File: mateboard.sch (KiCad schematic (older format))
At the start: 27 parts, among them J1 CONN_02X20, J2 CONN_02X20, P1 POWER, P2 DEVICE, P3 HOST, P4 microSD, Q1 BSS138, Q2 BSS138, Q3 BSS138, Q4 BSS138

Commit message: erc passed, sch first version
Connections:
- wire segments 188 -> 190
- no-connect marks 4 -> 3
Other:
- moved on the sheet: R1

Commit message: wip display connector
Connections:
- wire segments 190 -> 212
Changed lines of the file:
@@
 	1050 4525 900  4525
 Wire Wire Line
-	900  4500 900  4625
+	900  4500 900  4525
+Wire Wire Line
+	900  4525 900  4625
 Wire Wire Line
 	1350 4525 1525 4525
 Wire Wire Line
-	1525 4500 1525 4575
+	1525 4500 1525 4525
+Wire Wire Line
+	1525 4525 1525 4575
 $Sheet
 S 2600 4050 1250 1650
@@
 Connection ~ 9100 700
 Wire Wire Line
-	8625 700  9300 700
+	8625 700  8700 700
+Wire Wire Line
+	8700 700  8800 700
+Wire Wire Line
+	8800 700  8900 700
+Wire Wire Line
+	8900 700  9000 700
+Wire Wire Line
+	9000 700  9100 700
+Wire Wire Line
+	9100 700  9200 700
+Wire Wire Line
+	9200 700  9300 700
 Wire Wire Line
 	9200 700  9200 825
@@
 	9300 1125 9300 1175
 Wire Wire Line
-	8150 1175 9375 1175
-Wire Wire Line
-	8150 1275 9375 1275
+	8150 1175 9300 1175
+Wire Wire Line
+	9300 1175 9375 1175
+Wire Wire Line
+	8150 1275 9200 1275
+Wire Wire Line
+	9200 1275 9375 1275
 Wire Wire Line
 	9200 1275 9200 1125
 Wire Wire Line
-	8150 1375 9375 1375
+	8150 1375 9100 1375
+Wire Wire Line
+	9100 1375 9375 1375
 Wire Wire Line
 	9100 1375 9100 1125
@@
 	8700 1475 8700 700
 Wire Wire Line
-	8150 1575 9375 1575
+	8150 1575 9000 1575
+Wire Wire Line
+	9000 1575 9375 1575
 Wire Wire Line
 	9000 1575 9000 1125
@@
 $EndComp
 Wire Wire Line
-	9300 1675 9300 2175
+	9300 1675 9300 2125
+Wire Wire Line
+	9300 2125 9300 2175
 Wire Wire Line
 	9300 1675 9375 1675
 Wire Wire Line
-	8150 1775 9375 1775
+	8150 1775 8900 1775
+Wire Wire Line
+	8900 1775 9375 1775
 Wire Wire Line
 	8900 1775 8900 1125
 Wire Wire Line
-	8150 1875 9375 1875
+	8150 1875 8800 1875
+Wire Wire Line
+	8800 1875 9375 1875
 Wire Wire Line
 	8800 1875 8800 1125
@@
 Connection ~ 8700 700
 Wire Wire Line
-	8625 1125 8625 3425
+	8625 1125 8625 2025
+Wire Wire Line
+	8625 2025 8625 3425
 Wire Wire Line
 	9375 2125 9300 2125
@@
 	6800 3425 6900 3425
 Wire Wire Line
-	5850 2325 5850 3425
+	5850 2325 5850 3050
+Wire Wire Line
+	5850 3050 5850 3425
 Wire Wire Line
 	5850 2325 5725 2325
@@
 I2C0_SCL
 $Sheet
-S 6900 5650 1250 700
+S 6900 5650 1250 800
 U 58BD360A
-F0 "Boot Config" 60
+F0 "Boot Config-LCD" 60
 F1 "sysboot.sch" 60
 F2 "GPIO2_23" B R 8150 5850 60
@@
 F4 "GPIO2_24" B R 8150 5950 60
 F5 "GPIO2_25" B R 8150 6050 60
+F6 "HDMI_INT" O L 6900 5750 60
+F7 "CSDA" B L 6900 5950 60
+F8 "CSCL" I L 6900 6050 60
+F9 "ACLK" I R 8150 6150 60
+F10 "AP0" I R 8150 6250 60
+F11 "AP1" I R 8150 6350 60
+F12 "HDMICLK_DIS" I L 6900 5850 60
 $EndSheet
 Wire Wire Line
@@
 GPIO1_16
 Wire Wire Line
-	6900 2900 6475 2900
+	6050 2900 6900 2900
 Text Label 6475 2900 0    60   ~ 0
 GPIO1_27
 Wire Wire Line
-	6900 3000 6475 3000
+	6150 3000 6900 3000
 Text Label 6475 3000 0    60   ~ 0
 GPIO1_25
@@
 USB1_VBUS
 Wire Wire Line
-	9950 5525 9450 5525
+	9950 5525 9900 5525
+Wire Wire Line
+	9900 5525 9450 5525
 Text Label 9450 5525 0    60   ~ 0
 VBAT
@@
 UART4_TXD
 $Comp
-L GNDD #PWR?
+L GNDD #PWR042
 U 1 1 58C8D040
 P 9950 5425
-F 0 "#PWR?" H 9950 5175 50  0001 C CNN
+F 0 "#PWR042" H 9950 5175 50  0001 C CNN
 F 1 "GNDD" V 9950 5200 50  0000 C CNN
 F 2 "" H 9950 5425 50  0000 C CNN
@@
 	0    1    1    0
 $EndComp
+Wire Wire Line
+	6900 5750 6150 5750
+Wire Wire Line
+	6150 5750 6150 3000
+Wire Wire Line
+	6050 2900 6050 5850
+Wire Wire Line
+	6050 5850 6900 5850
 $EndSCHEMATC

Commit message: add display connector, bom generated, sch second version
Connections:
- wire segments 212 -> 202
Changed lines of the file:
@@
 	1050 4525 900  4525
 Wire Wire Line
-	900  4500 900  4525
-Wire Wire Line
-	900  4525 900  4625
+	900  4500 900  4625
 Wire Wire Line
 	1350 4525 1525 4525
 Wire Wire Line
-	1525 4500 1525 4525
-Wire Wire Line
-	1525 4525 1525 4575
+	1525 4500 1525 4575
 $Sheet
 S 2600 4050 1250 1650
@@
 F10 "GPIO0_7" B R 5725 1225 60
 F11 "CLKOUT2" O R 5725 2325 60
+F12 "CLKOUT1" O R 5725 2225 60
 $EndSheet
 $Sheet
@@
 Connection ~ 9100 700
 Wire Wire Line
-	8625 700  8700 700
-Wire Wire Line
-	8700 700  8800 700
-Wire Wire Line
-	8800 700  8900 700
-Wire Wire Line
-	8900 700  9000 700
-Wire Wire Line
-	9000 700  9100 700
-Wire Wire Line
-	9100 700  9200 700
-Wire Wire Line
-	9200 700  9300 700
+	8625 700  9300 700
 Wire Wire Line
 	9200 700  9200 825
@@
 	9300 1125 9300 1175
 Wire Wire Line
-	8150 1175 9300 1175
-Wire Wire Line
-	9300 1175 9375 1175
-Wire Wire Line
-	8150 1275 9200 1275
-Wire Wire Line
-	9200 1275 9375 1275
+	8150 1175 9375 1175
+Wire Wire Line
+	8150 1275 9375 1275
 Wire Wire Line
 	9200 1275 9200 1125
 Wire Wire Line
-	8150 1375 9100 1375
-Wire Wire Line
-	9100 1375 9375 1375
+	8150 1375 9375 1375
 Wire Wire Line
 	9100 1375 9100 1125
@@
 	8700 1475 8700 700
 Wire Wire Line
-	8150 1575 9000 1575
-Wire Wire Line
-	9000 1575 9375 1575
+	8150 1575 9375 1575
 Wire Wire Line
 	9000 1575 9000 1125
@@
 $EndComp
 Wire Wire Line
-	9300 1675 9300 2125
-Wire Wire Line
-	9300 2125 9300 2175
+	9300 1675 9300 2175
 Wire Wire Line
 	9300 1675 9375 1675
 Wire Wire Line
-	8150 1775 8900 1775
-Wire Wire Line
-	8900 1775 9375 1775
+	8150 1775 9375 1775
 Wire Wire Line
 	8900 1775 8900 1125
 Wire Wire Line
-	8150 1875 8800 1875
-Wire Wire Line
-	8800 1875 9375 1875
+	8150 1875 9375 1875
 Wire Wire Line
 	8800 1875 8800 1125
@@
 Connection ~ 8700 700
 Wire Wire Line
-	8625 1125 8625 2025
-Wire Wire Line
-	8625 2025 8625 3425
+	8625 1125 8625 3425
 Wire Wire Line
 	9375 2125 9300 2125
@@
 	6800 3425 6900 3425
 Wire Wire Line
-	5850 2325 5850 3050
-Wire Wire Line
-	5850 3050 5850 3425
+	5850 2325 5850 3425
 Wire Wire Line
 	5850 2325 5725 2325
@@
 F11 "AP1" I R 8150 6350 60
 F12 "HDMICLK_DIS" I L 6900 5850 60
+F13 "OSC_IN" I L 6900 6150 60
 $EndSheet
 Wire Wire Line
@@
 AIN6
 Wire Wire Line
-	8150 5750 8575 5750
-Text Label 8575 5750 2    60   ~ 0
+	8150 5750 8650 5750
+Text Label 8650 5750 2    60   ~ 0
 GPIO2_22
 Wire Wire Line
-	8150 5850 8575 5850
-Text Label 8575 5850 2    60   ~ 0
+	8150 5850 8650 5850
+Text Label 8650 5850 2    60   ~ 0
 GPIO2_23
 Wire Wire Line
-	8150 5950 8575 5950
-Text Label 8575 5950 2    60   ~ 0
+	8150 5950 8650 5950
+Text Label 8650 5950 2    60   ~ 0
 GPIO2_24
 Wire Wire Line
-	8150 6050 8575 6050
-Text Label 8575 6050 2    60   ~ 0
+	8150 6050 8650 6050
+Text Label 8650 6050 2    60   ~ 0
 GPIO2_25
 $Comp
@@
 USB1_VBUS
 Wire Wire Line
-	9950 5525 9900 5525
-Wire Wire Line
-	9900 5525 9450 5525
+	9450 5525 9950 5525
 Text Label 9450 5525 0    60   ~ 0
 VBAT
@@
 Wire Wire Line
 	6050 5850 6900 5850
+Wire Wire Line
+	6900 5950 6400 5950
+Wire Wire Line
+	6400 6050 6900 6050
+Text Label 6400 6050 0    60   ~ 0
+I2C0_SDA
+Text Label 6400 5950 0    60   ~ 0
+I2C0_SCL
+Wire Wire Line
+	5725 2225 6250 2225
+Wire Wire Line
+	6250 2225 6250 6150
+Wire Wire Line
+	6250 6150 6900 6150
+Text Label 8650 6150 2    60   ~ 0
+SPI1_SCLK
+Wire Wire Line
+	8650 6150 8150 6150
+Text Label 8650 6250 2    60   ~ 0
+SPI1_MISO
+Wire Wire Line
+	8650 6250 8150 6250
+Text Label 8650 6350 2    60   ~ 0
+SPI1_CS0
+Wire Wire Line
+	8650 6350 8150 6350
 $EndSCHEMATC

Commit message: wip sch
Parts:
- removed D1, D2, D3, D4: LTST-C191TBKT, symbol LED
- removed Q1, Q2, Q3, Q4: BSS138, TO_SOT_Packages_SMD:SOT-23, symbol BSS138
- removed R2, R3, R4, R5: 1k, symbol R
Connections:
- wire segments 202 -> 198
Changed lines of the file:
@@
 LIBS:74lvc1g07dck
 LIBS:wl1835modgbmoct
+LIBS:osd335x
 LIBS:mateboard-cache
 EELAYER 25 0
@@
 	5850 3425 6500 3425
 Connection ~ 5850 3050
-$Comp
-L BSS138 Q1
-U 1 1 58BD6236
-P 1125 7300
-F 0 "Q1" H 1325 7375 50  0000 L CNN
-F 1 "BSS138" H 1325 7300 50  0000 L CNN
-F 2 "TO_SOT_Packages_SMD:SOT-23" H 1325 7225 50  0001 L CIN
-F 3 "" H 1125 7300 50  0001 L CNN
-	1    1125 7300
-	1    0    0    -1
-$EndComp
-Wire Wire Line
-	625  7350 925  7350
-$Comp
-L GNDD #PWR014
-U 1 1 58BD623E
-P 1225 7500
-F 0 "#PWR014" H 1225 7250 50  0001 C CNN
-F 1 "GNDD" H 1225 7350 50  0000 C CNN
-F 2 "" H 1225 7500 50  0000 C CNN
-F 3 "" H 1225 7500 50  0000 C CNN
-	1    1225 7500
-	1    0    0    -1
-$EndComp
-$Comp
-L LED D1
-U 1 1 58BD6244
-P 1225 6950
-F 0 "D1" H 1225 7150 50  0000 C CNN
-F 1 "LTST-C191TBKT" H 1225 7075 50  0000 C CNN
-F 2 "" H 1225 6950 50  0000 C CNN
-F 3 "" H 1225 6950 50  0000 C CNN
-	1    1225 6950
-	0    -1   -1   0
-$EndComp
-$Comp
-L R R2
-U 1 1 58BD624B
-P 1225 6650
-F 0 "R2" V 1275 6800 50  0000 C CNN
-F 1 "1k" V 1225 6650 50  0000 C CNN
-F 2 "" V 1155 6650 50  0000 C CNN
-F 3 "" H 1225 6650 50  0000 C CNN
-	1    1225 6650
-	1    0    0    -1
-$EndComp
-Text Label 625  7350 0    60   ~ 0
-USR0
-$Comp
-L VDD_3V3B #PWR015
-U 1 1 58BD685D
-P 1225 6500
-F 0 "#PWR015" H 1225 6350 50  0001 C CNN
-F 1 "VDD_3V3B" H 1225 6650 50  0000 C CNN
-F 2 "" H 1225 6500 50  0000 C CNN
-F 3 "" H 1225 6500 50  0000 C CNN
-	1    1225 6500
-	1    0    0    -1
-$EndComp
-$Comp
-L BSS138 Q2
-U 1 1 58BDAD53
-P 2125 7300
-F 0 "Q2" H 2325 7375 50  0000 L CNN
-F 1 "BSS138" H 2325 7300 50  0000 L CNN
-F 2 "TO_SOT_Packages_SMD:SOT-23" H 2325 7225 50  0001 L CIN
-F 3 "" H 2125 7300 50  0001 L CNN
-	1    2125 7300
-	1    0    0    -1
-$EndComp
-Wire Wire Line
-	1625 7350 1925 7350
-$Comp
-L GNDD #PWR016
-U 1 1 58BDAD5A
-P 2225 7500
-F 0 "#PWR016" H 2225 7250 50  0001 C CNN
-F 1 "GNDD" H 2225 7350 50  0000 C CNN
-F 2 "" H 2225 7500 50  0000 C CNN
-F 3 "" H 2225 7500 50  0000 C CNN
-	1    2225 7500
-	1    0    0    -1
-$EndComp
-$Comp
-L LED D2
-U 1 1 58BDAD60
-P 2225 6950
-F 0 "D2" H 2225 7150 50  0000 C CNN
-F 1 "LTST-C191TBKT" H 2225 7075 50  0000 C CNN
-F 2 "" H 2225 6950 50  0000 C CNN
-F 3 "" H 2225 6950 50  0000 C CNN
-	1    2225 6950
-	0    -1   -1   0
-$EndComp
-$Comp
-L R R3
-U 1 1 58BDAD66
-P 2225 6650
-F 0 "R3" V 2275 6800 50  0000 C CNN
-F 1 "1k" V 2225 6650 50  0000 C CNN
-F 2 "" V 2155 6650 50  0000 C CNN
-F 3 "" H 2225 6650 50  0000 C CNN
-	1    2225 6650
-	1    0    0    -1
-$EndComp
-Text Label 1625 7350 0    60   ~ 0
-USR1
-$Comp
-L VDD_3V3B #PWR017
-U 1 1 58BDAD6D
-P 2225 6500
-F 0 "#PWR017" H 2225 6350 50  0001 C CNN
-F 1 "VDD_3V3B" H 2225 6650 50  0000 C CNN
-F 2 "" H 2225 6500 50  0000 C CNN
-F 3 "" H 2225 6500 50  0000 C CNN
-	1    2225 6500
-	1    0    0    -1
-$EndComp
-$Comp
-L BSS138 Q3
-U 1 1 58BDC8A1
-P 3150 7300
-F 0 "Q3" H 3350 7375 50  0000 L CNN
-F 1 "BSS138" H 3350 7300 50  0000 L CNN
-F 2 "TO_SOT_Packages_SMD:SOT-23" H 3350 7225 50  0001 L CIN
-F 3 "" H 3150 7300 50  0001 L CNN
-	1    3150 7300
-	1    0    0    -1
-$EndComp
-Wire Wire Line
-	2650 7350 2950 7350
-$Comp
-L GNDD #PWR018
-U 1 1 58BDC8A8
-P 3250 7500
-F 0 "#PWR018" H 3250 7250 50  0001 C CNN
-F 1 "GNDD" H 3250 7350 50  0000 C CNN
-F 2 "" H 3250 7500 50  0000 C CNN
-F 3 "" H 3250 7500 50  0000 C CNN
-	1    3250 7500
-	1    0    0    -1
-$EndComp
-$Comp
-L LED D3
-U 1 1 58BDC8AE
-P 3250 6950
-F 0 "D3" H 3250 7150 50  0000 C CNN
-F 1 "LTST-C191TBKT" H 3250 7075 50  0000 C CNN
-F 2 "" H 3250 6950 50  0000 C CNN
-F 3 "" H 3250 6950 50  0000 C CNN
-	1    3250 6950
-	0    -1   -1   0
-$EndComp
-$Comp
-L R R4
-U 1 1 58BDC8B4
-P 3250 6650
-F 0 "R4" V 3300 6800 50  0000 C CNN
-F 1 "1k" V 3250 6650 50  0000 C CNN
-F 2 "" V 3180 6650 50  0000 C CNN
-F 3 "" H 3250 6650 50  0000 C CNN
-	1    3250 6650
-	1    0    0    -1
-$EndComp
-Text Label 2650 7350 0    60   ~ 0
-USR2
-$Comp
-L VDD_3V3B #PWR019
-U 1 1 58BDC8BB
-P 3250 6500
-F 0 "#PWR019" H 3250 6350 50  0001 C CNN
-F 1 "VDD_3V3B" H 3250 6650 50  0000 C CNN
-F 2 "" H 3250 6500 50  0000 C CNN
-F 3 "" H 3250 6500 50  0000 C CNN
-	1    3250 6500
-	1    0    0    -1
-$EndComp
-$Comp
-L BSS138 Q4
-U 1 1 58BDC8C1
-P 4150 7300
-F 0 "Q4" H 4350 7375 50  0000 L CNN
-F 1 "BSS138" H 4350 7300 50  0000 L CNN
-F 2 "TO_SOT_Packages_SMD:SOT-23" H 4350 7225 50  0001 L CIN
-F 3 "" H 4150 7300 50  0001 L CNN
-	1    4150 7300
-	1    0    0    -1
-$EndComp
-Wire Wire Line
-	3650 7350 3950 7350
-$Comp
-L GNDD #PWR020
-U 1 1 58BDC8C8
-P 4250 7500
-F 0 "#PWR020" H 4250 7250 50  0001 C CNN
-F 1 "GNDD" H 4250 7350 50  0000 C CNN
-F 2 "" H 4250 7500 50  0000 C CNN
-F 3 "" H 4250 7500 50  0000 C CNN
-	1    4250 7500
-	1    0    0    -1
-$EndComp
-$Comp
-L LED D4
-U 1 1 58BDC8CE
-P 4250 6950
-F 0 "D4" H 4250 7150 50  0000 C CNN
-F 1 "LTST-C191TBKT" H 4250 7075 50  0000 C CNN
-F 2 "" H 4250 6950 50  0000 C CNN
-F 3 "" H 4250 6950 50  0000 C CNN
-	1    4250 6950
-	0    -1   -1   0
-$EndComp
-$Comp
-L R R5
-U 1 1 58BDC8D4
-P 4250 6650
-F 0 "R5" V 4300 6800 50  0000 C CNN
-F 1 "1k" V 4250 6650 50  0000 C CNN
-F 2 "" V 4180 6650 50  0000 C CNN
-F 3 "" H 4250 6650 50  0000 C CNN
-	1    4250 6650
-	1    0    0    -1
-$EndComp
-Text Label 3650 7350 0    60   ~ 0
-USR3
-$Comp
-L VDD_3V3B #PWR021
-U 1 1 58BDC8DB
-P 4250 6500
-F 0 "#PWR021" H 4250 6350 50  0001 C CNN
-F 1 "VDD_3V3B" H 4250 6650 50  0000 C CNN
-F 2 "" H 4250 6500 50  0000 C CNN
-F 3 "" H 4250 6500 50  0000 C CNN
-	1    4250 6500
-	1    0    0    -1
-$EndComp
 Wire Wire Line
 	8150 2050 8400 2050

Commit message: wip sys and power
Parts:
- removed J1, J2: CONN_02X20, symbol CONN_02X20
- removed P1: POWER, symbol USB_OTG-RESCUE-mateboard
- removed P2: DEVICE, symbol USB_OTG-RESCUE-mateboard
- removed P3: HOST, symbol USB_A-RESCUE-mateboard
- removed P4: microSD, symbol microSD
- removed R1: 0.1, Resistors_SMD:R_0805, symbol R
- removed R10, R11, R12, R13, R7, R8, R9: 10k, symbol R
- removed R6: 0R, symbol R
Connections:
- net labels removed: AIN0, AIN1, AIN2, AIN3, AIN4, AIN5, AIN6, GNDA, GNDD, GNDSHIELD, GPIO0_26, GPIO0_27, GPIO0_7, GPIO1_12, GPIO1_13, GPIO1_14, GPIO1_15, GPIO1_16, GPIO1_17, GPIO1_25, GPIO1_27, GPIO1_28, GPIO1_29, GPIO2_0, GPIO2_1, GPIO2_22, GPIO2_23, GPIO2_24, GPIO2_25, GPIO3_19, GPIO3_21, I2C1_SCL, I2C1_SDA, I2C2_SCL, I2C2_SDA, MMC0_CD, PWM1A, PWM1B, PWM2A, PWM2B, SPI1_CS0, SPI1_MISO, SPI1_MOSI, SPI1_SCLK, SYS_5V, TIMER4, TIMER5, TIMER6, TIMER7, UART0_RXD, UART0_TXD, UART1_RXD, UART1_TXD, UART2_RXD, UART2_TXD, UART4_RXD, UART4_TXD, USB0_DM, USB0_DP, USB0_ID, USB1_DM, USB1_DP, USB1_OCn, USB1_VBUS, USB_DC, USR0, USR1, USR2, USR3, VDD_3V3B, VDD_5V, VSS_RTC
- wire segments 198 -> 11
- no-connect marks 3 -> 0

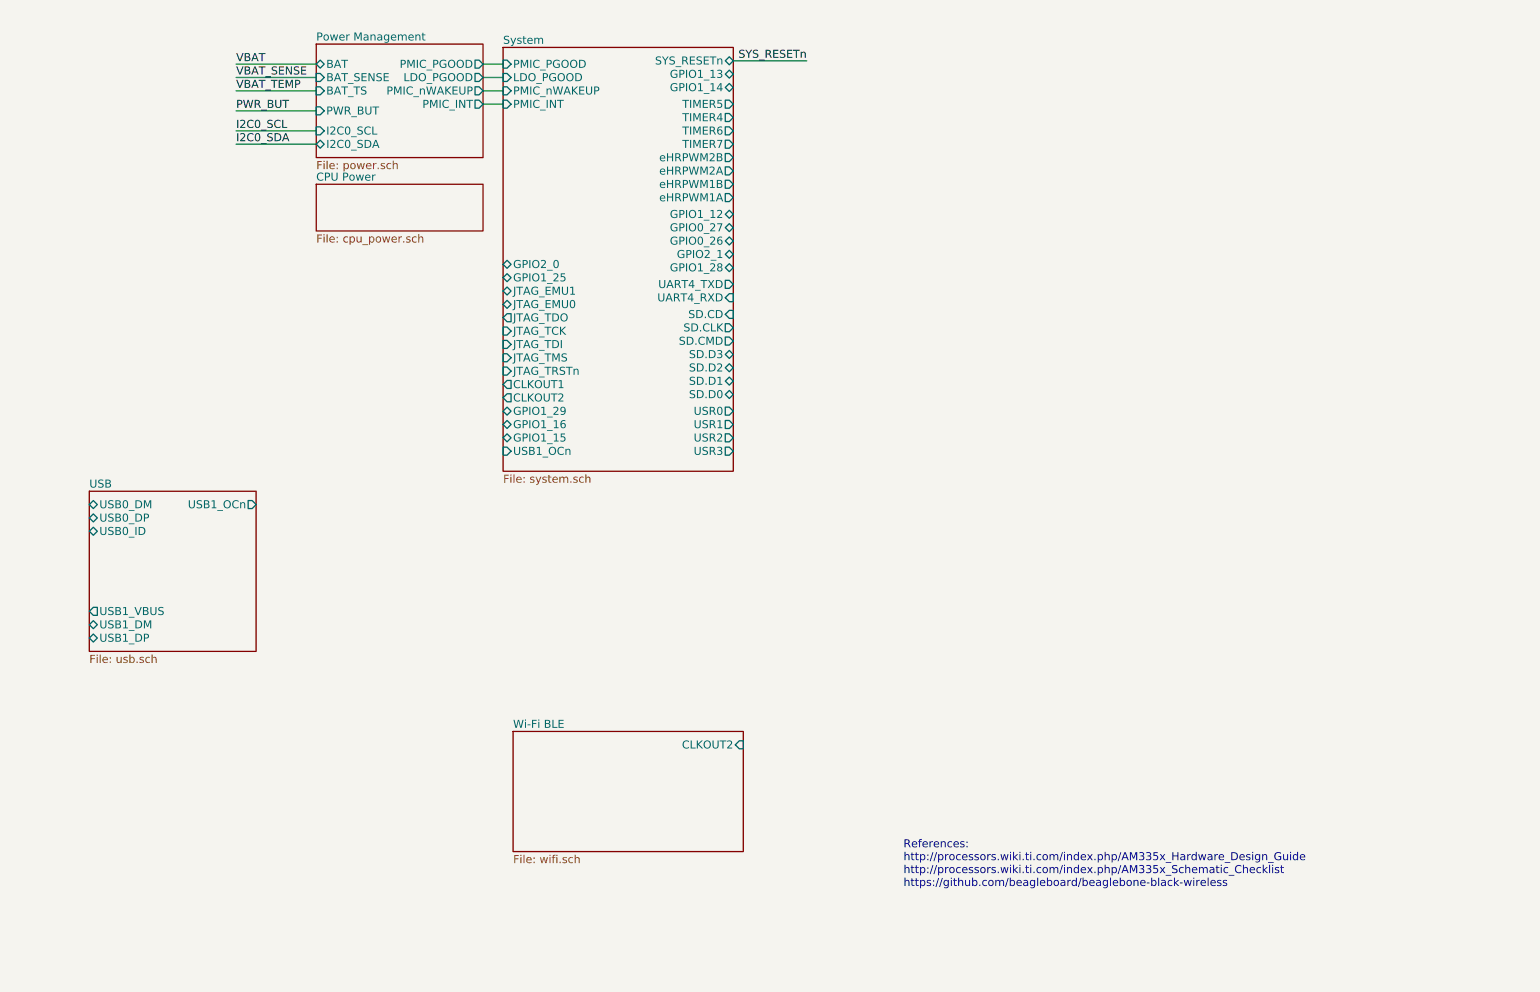
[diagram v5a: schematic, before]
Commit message: only io connectors remaining
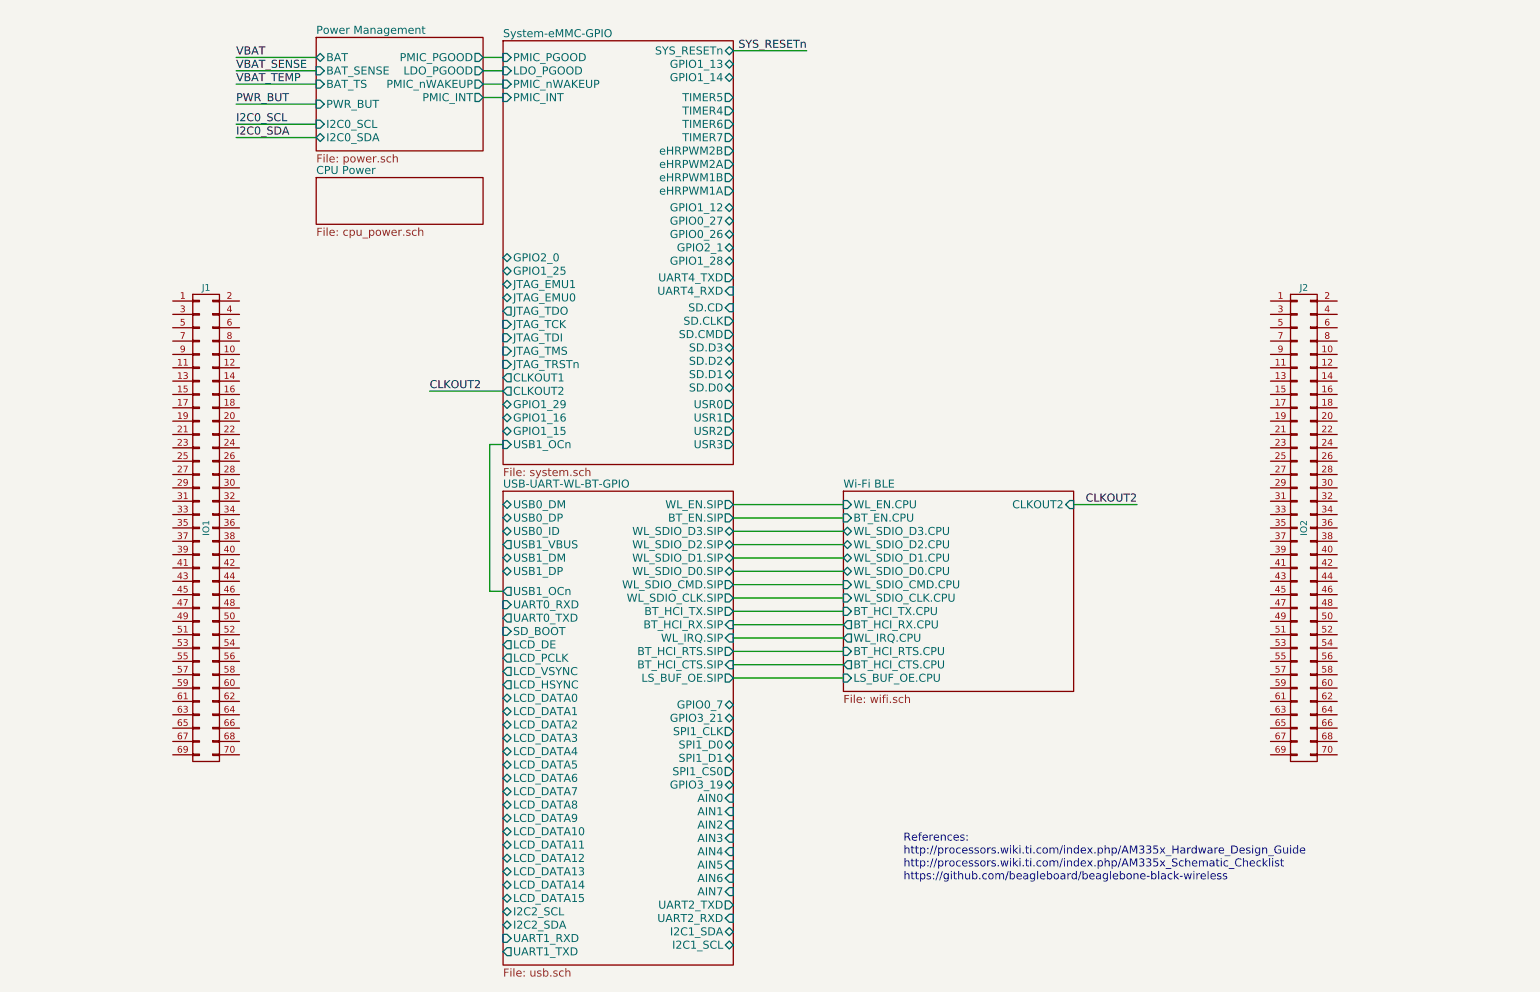
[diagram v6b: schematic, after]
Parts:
- added J1: IO1, symbol CONN_02X35
- added J2: IO2, symbol CONN_02X35
